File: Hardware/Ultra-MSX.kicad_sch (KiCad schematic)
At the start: 8 parts

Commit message: Routed the VDP-board further, as well as making it a 4-layer board - also added an exception in the gitignore, for big images.
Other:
- sheet Audio renamed AUDIO
- sheet Audio Amplifiers renamed AUDIO AMPLIFIERS
- sheet MSX Engine renamed MSX ENGINE
- sheet Memory renamed MEMORY
- sheet Peripherals renamed PERIPHERALS
- sheet Power renamed POWER
- sheet Processor renamed PROCESSOR
- sheet Slots renamed SLOTS
- sheet VDP renamed VIDEO
- sheet MSX ENGINE ports: added AUX+, AUX-, CC1/HPD, ENG_~{INT}, SSRX+, SSRX-, SSTX+, SSTX-, USB1_D+, USB1_D-, USB2_D+, USB2_D-; removed ENG_~{INT}/INIT
- sheet PERIPHERALS ports: added AUX+, AUX-, CC1/HPD, CSYNC, SSRX+, SSRX-, SSTX+, SSTX-, USB1_D+, USB1_D-, USB2_D+, USB2_D-; removed KEY_CLICK, SYNC
- sheet PROCESSOR ports: added ENG_~{INT}; removed ENG_~{INT}/INIT
- sheet VIDEO ports: added CSYNC; removed SYNC

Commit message: Finished the VDP-board, finished up the mixer-section, removed the buffer-pins from the FPGA, and instead added external buffers for the slots, designed a marquee-block with the Ultra-MSX logo, designed the logotype, andmultiple other changes.
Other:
- sheet AUDIO ports: added A[0..31]; removed none
- sheet AUDIO AMPLIFIERS ports: added I2C_AD1, I2C_AD2, I2C_AD3, I2C_SCL, I2C_SDA, I2C_~{WP}, SLT3_SND_L, SLT3_SND_R; removed SLT3_SND
- sheet MSX ENGINE ports: added I2C_AD1, I2C_AD2, I2C_AD3, I2C_SCL, I2C_SDA, I2C_~{WP}, SLT_DIR, ~{MREQ}, ~{RFSH}; removed BA[0..15], BD[0..7], B_CLK, ~{B_IORQ}, ~{B_M1}, ~{B_MREQ}, ~{B_RD}, ~{B_RESET}, ~{B_RFSH}, ~{B_WR}
- sheet PERIPHERALS ports: added HSYNC, VSYNC; removed none
- sheet SLOTS ports: added A[0..31], CLK_BUS, D[0..15], SLT3_SND_L, SLT3_SND_R, SLT_DIR, ~{IORQ}, ~{M1}, ~{MREQ}, ~{RD}, ~{RESET}, ~{RFSH}, ~{WR}; removed BA[0..15], BD[0..7], B_CLK, SLT3_SND, ~{B_IORQ}, ~{B_M1}, ~{B_MREQ}, ~{B_RD}, ~{B_RESET}, ~{B_RFSH}, ~{B_WR}
- sheet VIDEO ports: added HSYNC, VSYNC; removed none
- moved on the sheet: Cart1, Cart2, Cart3, H1, H2, H3, H4, HS1

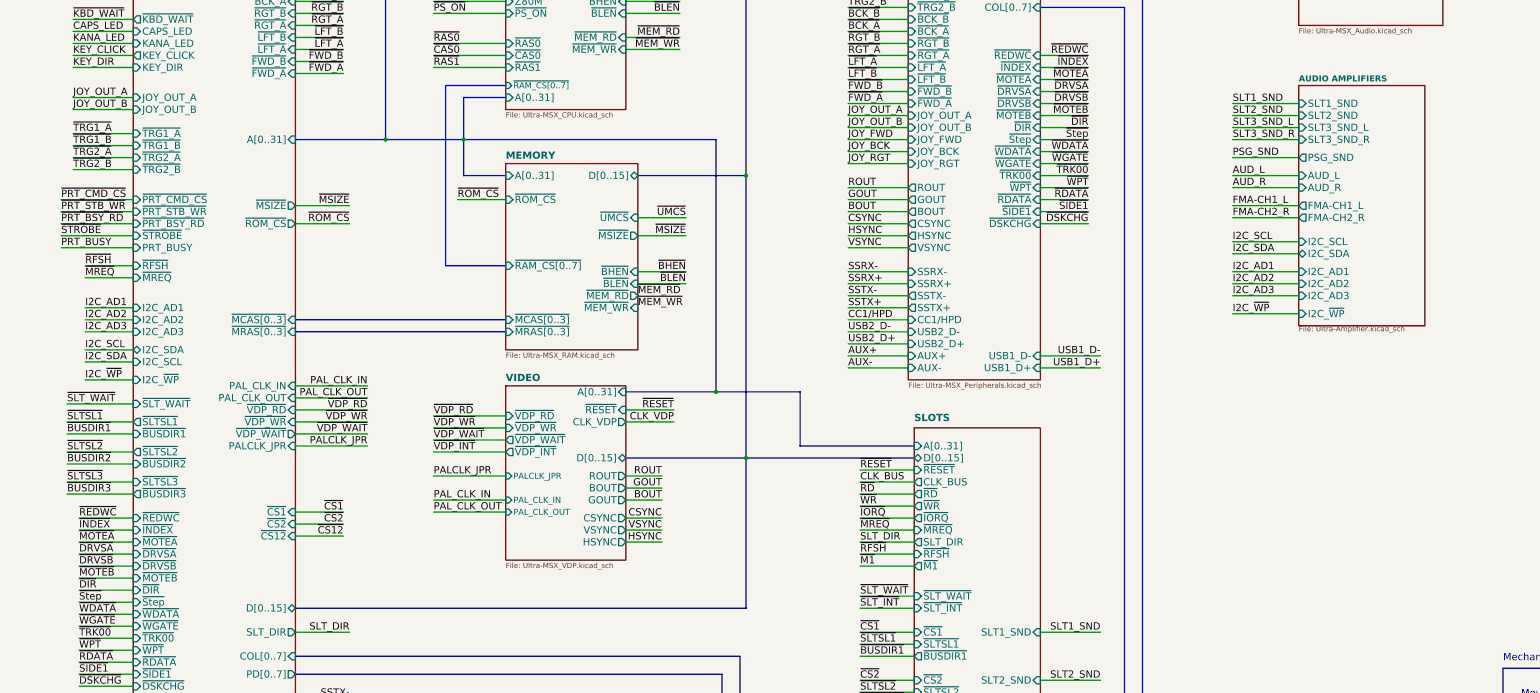
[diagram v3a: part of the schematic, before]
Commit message: Added SD-card slot, made basic 3d-model for sd-card slot, connected it up in the schematic, and numerous other tweaks.
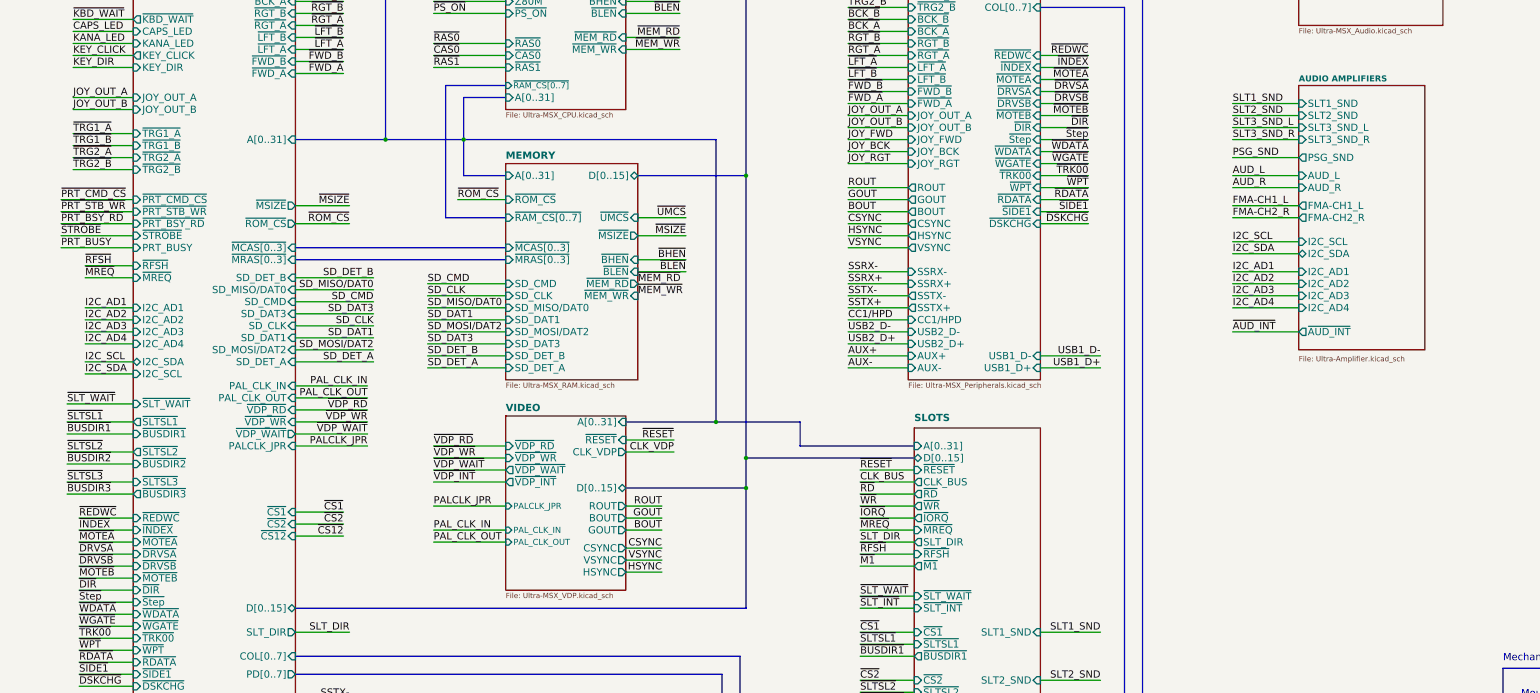
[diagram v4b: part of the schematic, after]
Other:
- sheet AUDIO AMPLIFIERS ports: added I2C_AD4, ~{AUD_INT}; removed I2C_~{WP}
- sheet MEMORY ports: added SD_CLK, SD_CMD, SD_DAT1, SD_DAT3, SD_DET_A, SD_DET_B, SD_MISO/DAT0, SD_MOSI/DAT2; removed none
- sheet MSX ENGINE ports: added I2C_AD4, SD_CLK, SD_CMD, SD_DAT1, SD_DAT3, SD_DET_A, SD_DET_B, SD_MISO/DAT0, SD_MOSI/DAT2; removed I2C_~{WP}

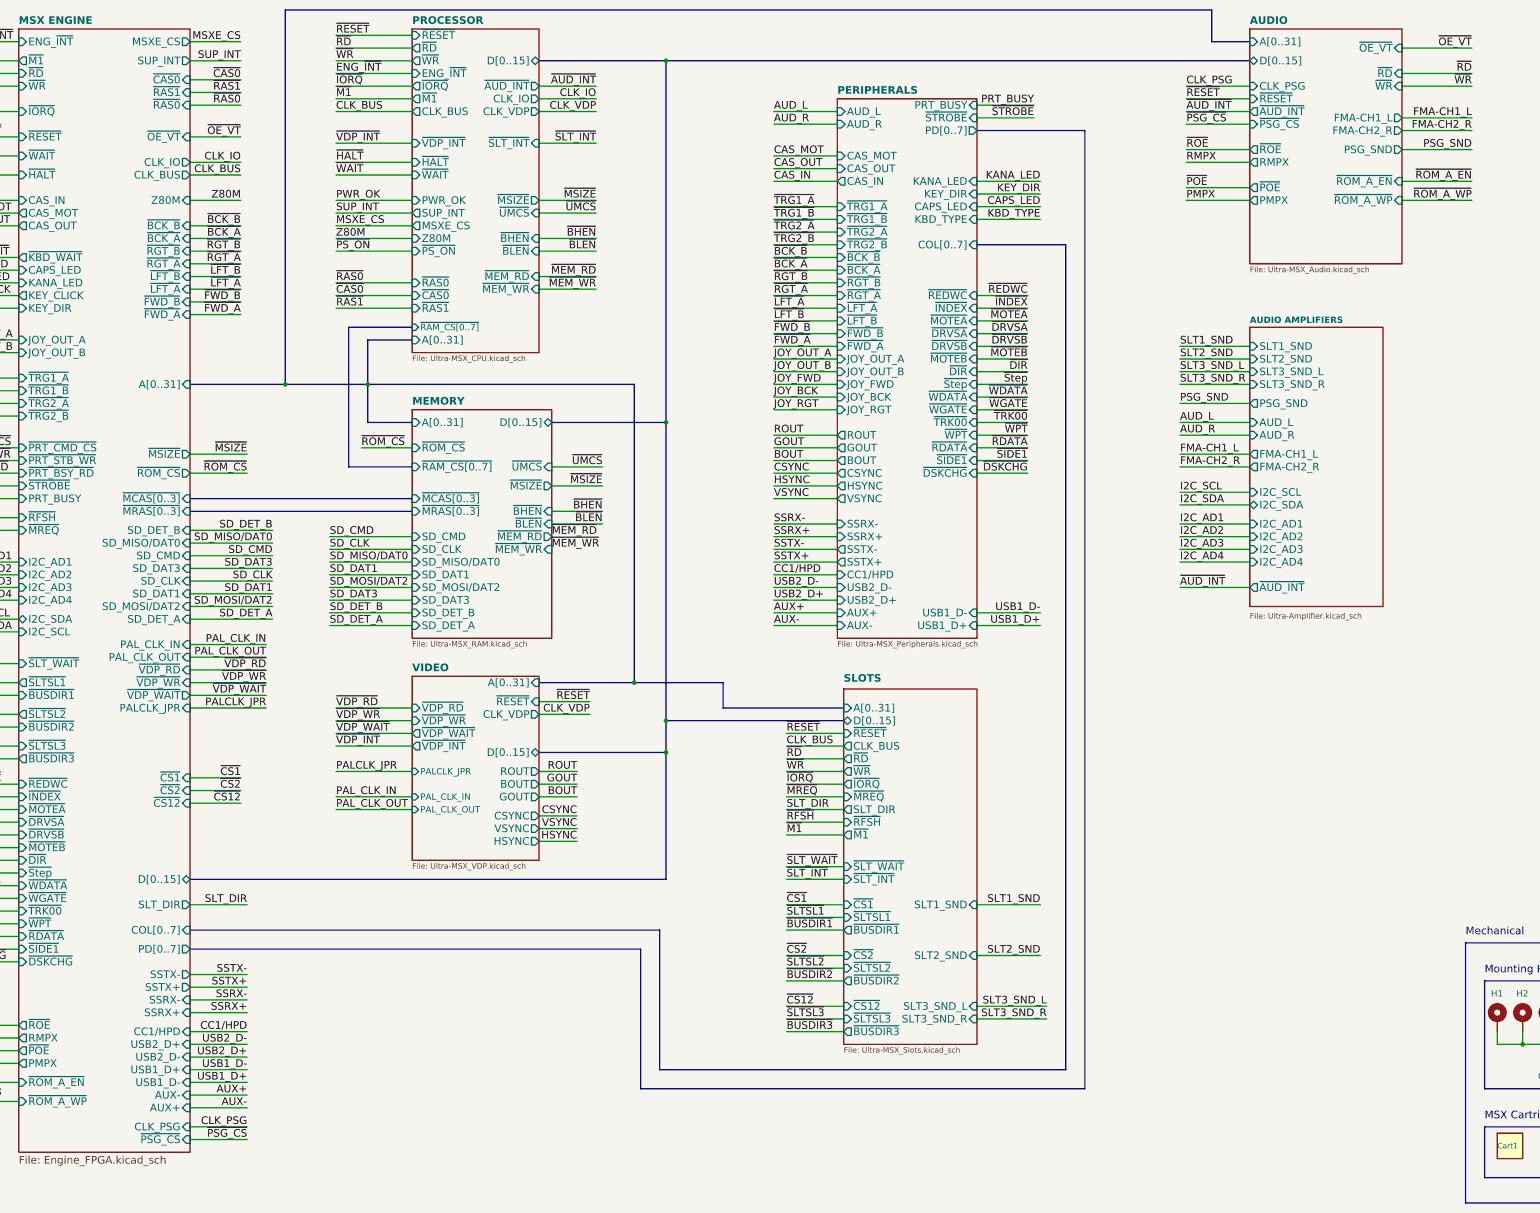
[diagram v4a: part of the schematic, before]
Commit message: Redesigned VDP-board to include a socket, increased it to 4 layers. Various clean-ups here and there. Improved the printer-port and joystick-port 3D-models. Improved the cooling-fin 3D-model, and added attachment-spring in 3D-model.
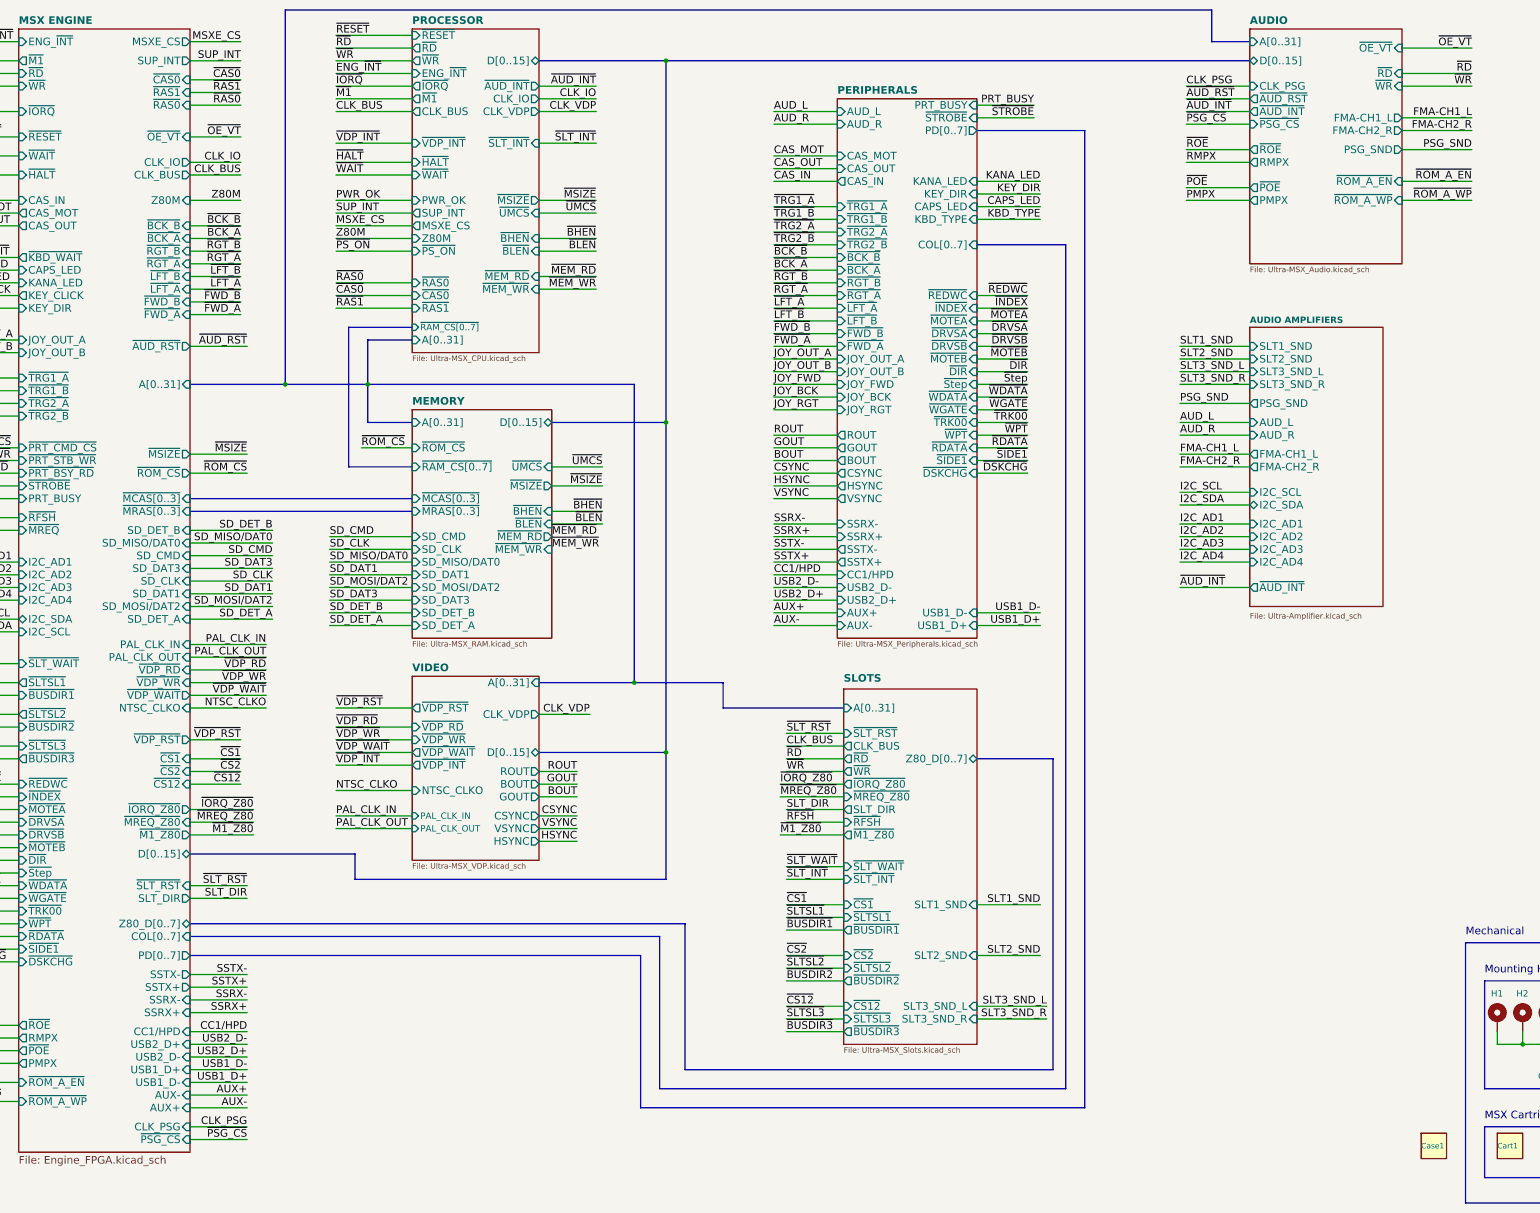
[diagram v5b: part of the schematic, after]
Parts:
- added Case1: MSX-DANv4-case_dummy, Ultra-MSX:DAN-Case-dummy, symbol Ultra-MSX:MSX-DANv4-case_dummy
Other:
- sheet AUDIO ports: added ~{AUD_RST}; removed ~{RESET}
- sheet MSX ENGINE ports: added NTSC_CLKO, Z80_D[0..7], ~{AUD_RST}, ~{IORQ_Z80}, ~{M1_Z80}, ~{MREQ_Z80}, ~{SLT_RST}, ~{VDP_RST}; removed PALCLK_JPR
- sheet SLOTS ports: added Z80_D[0..7], ~{IORQ_Z80}, ~{M1_Z80}, ~{MREQ_Z80}, ~{SLT_RST}; removed D[0..15], ~{IORQ}, ~{M1}, ~{MREQ}, ~{RESET}
- sheet VIDEO ports: added NTSC_CLKO, ~{VDP_RST}; removed PALCLK_JPR, ~{RESET}

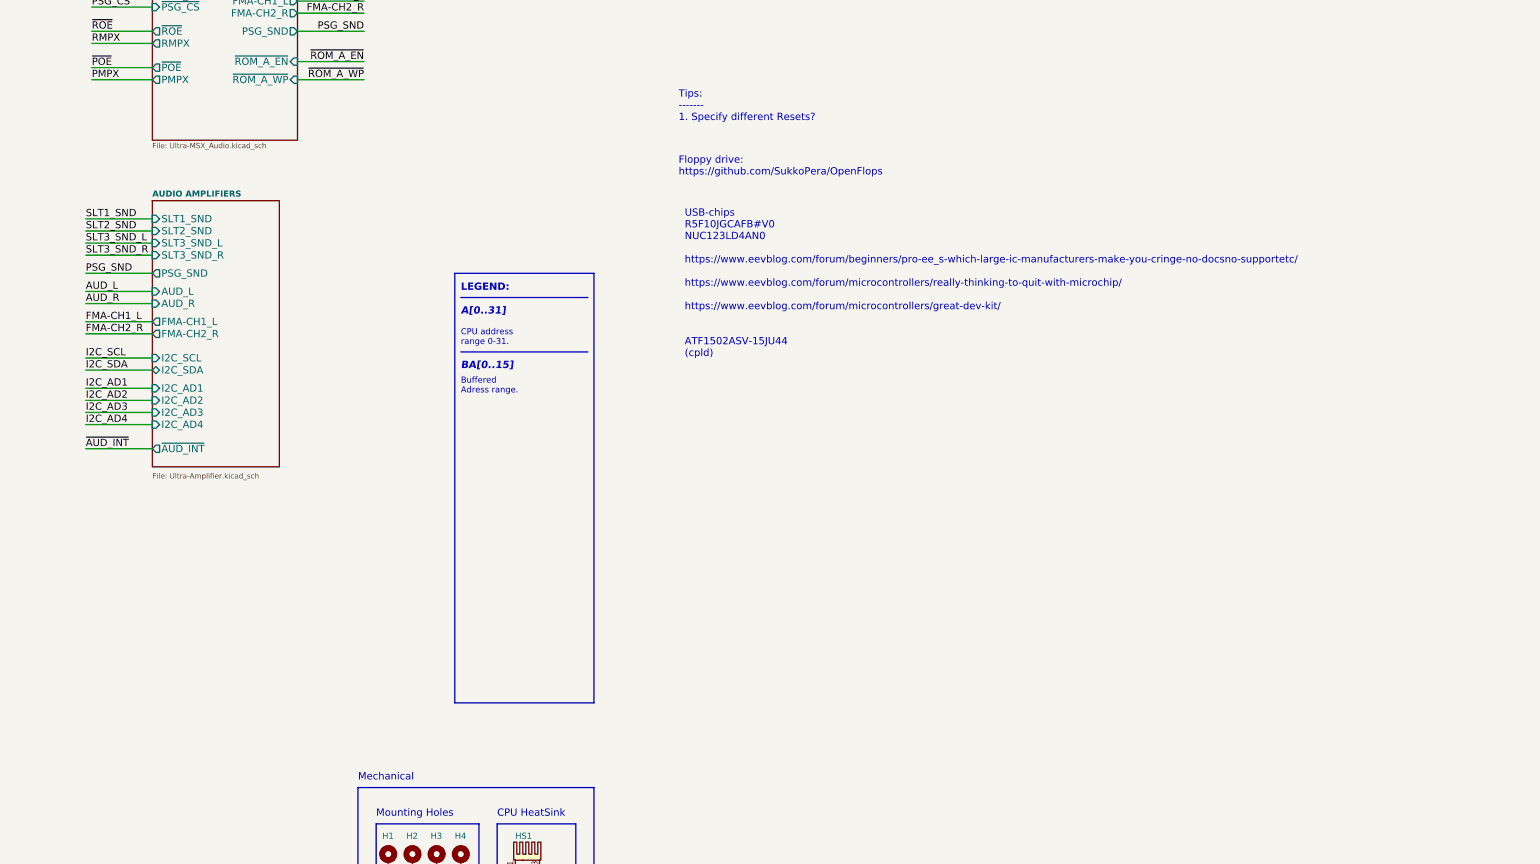
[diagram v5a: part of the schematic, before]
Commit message: Generated first PDF-files
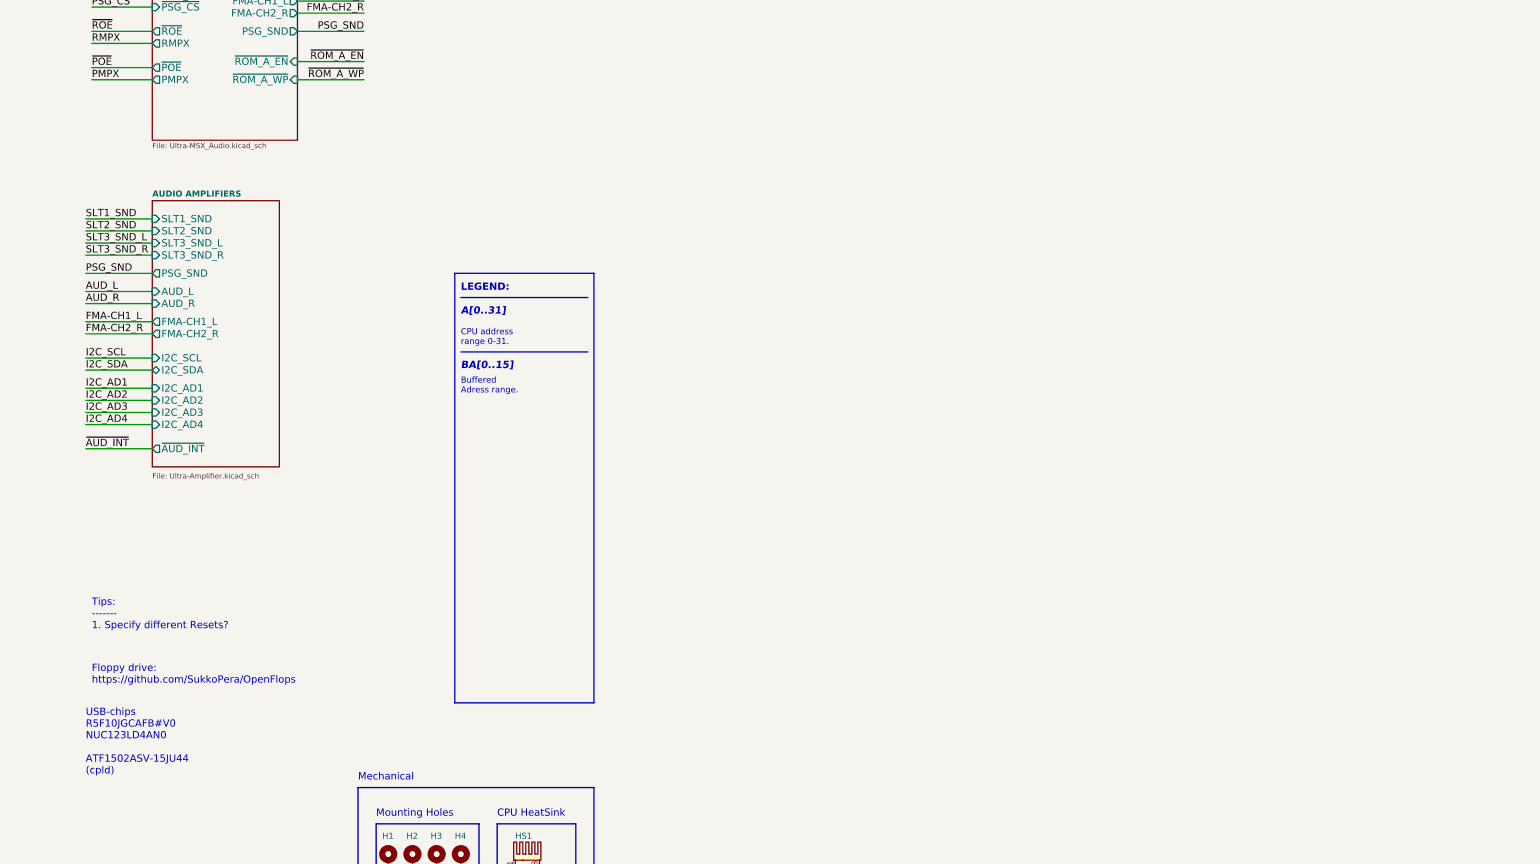
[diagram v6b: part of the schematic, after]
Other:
- note added: "USB-chips R5F10JGCAFB#V0 NUC123LD4AN0 ATF1502ASV-15JU44 (cpld)"
- note removed: "USB-chips R5F10JGCAFB#V0 NUC123LD4AN0 https://www.eevblog.com/forum/beginners/pro-ee_s-which-large-ic-manufacturers-make-you-cringe-no-docsno-supportetc/ https://www.eevblog.com/forum/microcontrollers/really-thinking-to-quit-with-microchip/ https://www.eevblog.com/forum/microcontrollers/great-dev-kit/ ATF1502ASV-15JU44 (cpld)"
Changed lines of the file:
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@@
     (effects (font (size 1.524 1.524) (thickness 0.3048) bold italic) (justify left bottom))
   )
-  (text "Tips:\n-------\n1. Specify different Resets?" (at 424.18 66.04 0)
+  (text "Tips:\n-------\n1. Specify different Resets?" (at 300.99 172.72 0)
     (effects (font (size 1.524 1.524)) (justify left bottom))
   )
@@
   )
   (text "Floppy drive:\nhttps://github.com/SukkoPera/OpenFlops"
-    (at 424.18 77.47 0)
+    (at 300.99 184.15 0)
     (effects (font (size 1.524 1.524)) (justify left bottom))
   )
@@
     (effects (font (size 1.524 1.524)) (justify left bottom))
   )
-  (text "USB-chips\nR5F10JGCAFB#V0\nNUC123LD4AN0\n\nhttps://www.eevblog.com/forum/beginners/pro-ee_s-which-large-ic-manufacturers-make-you-cringe-no-docsno-supportetc/\n\nhttps://www.eevblog.com/forum/microcontrollers/really-thinking-to-quit-with-microchip/\n\nhttps://www.eevblog.com/forum/microcontrollers/great-dev-kit/\n\n\nATF1502ASV-15JU44\n(cpld)\n"
-    (at 425.45 115.57 0)
+  (text "USB-chips\nR5F10JGCAFB#V0\nNUC123LD4AN0\n\nATF1502ASV-15JU44\n(cpld)\n"
+    (at 299.72 203.2 0)
     (effects (font (size 1.524 1.524)) (justify left bottom))
   )
@@
       (reference "J17") (unit 1) (value "X2GS") (footprint "Ultra-MSX:X2GS")
     )
-    (path "/00000000-0000-0000-0000-00005bd9da3d/3103b352-d224-465c-b0f2-262dbe32c2d6"
-      (reference "J18") (unit 1) (value "Amphenol_L77HDE15SD1CH4RHNVGA") (footprint "LRJ:DSUB-Amphenol_L77HDE15SD1CH4RHNVGA")
-    )
-    (path "/00000000-0000-0000-0000-00005bd9da3d/d91bc45d-7ad2-45a0-a3b4-b7d87b19eb54"
-      (reference "J19") (unit 1) (value "Console5_SCART") (footprint "LRJ:SCART-21_Female_Horizontal_P1.905x2.54mm_EdgePinOffset10.7mm")
-    )
     (path "/00000000-0000-0000-0000-00005bd9d8c5/f1794f41-17f3-4d46-b361-5fbd727ffd48"
